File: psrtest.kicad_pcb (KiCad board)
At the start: 2 copper layers, 5 parts, among them J1 Conn_01x12, J2 Conn_01x12, J3 Conn_01x12, J4 Conn_01x12, U1 IS66WVE4M16EBLL-70BLI

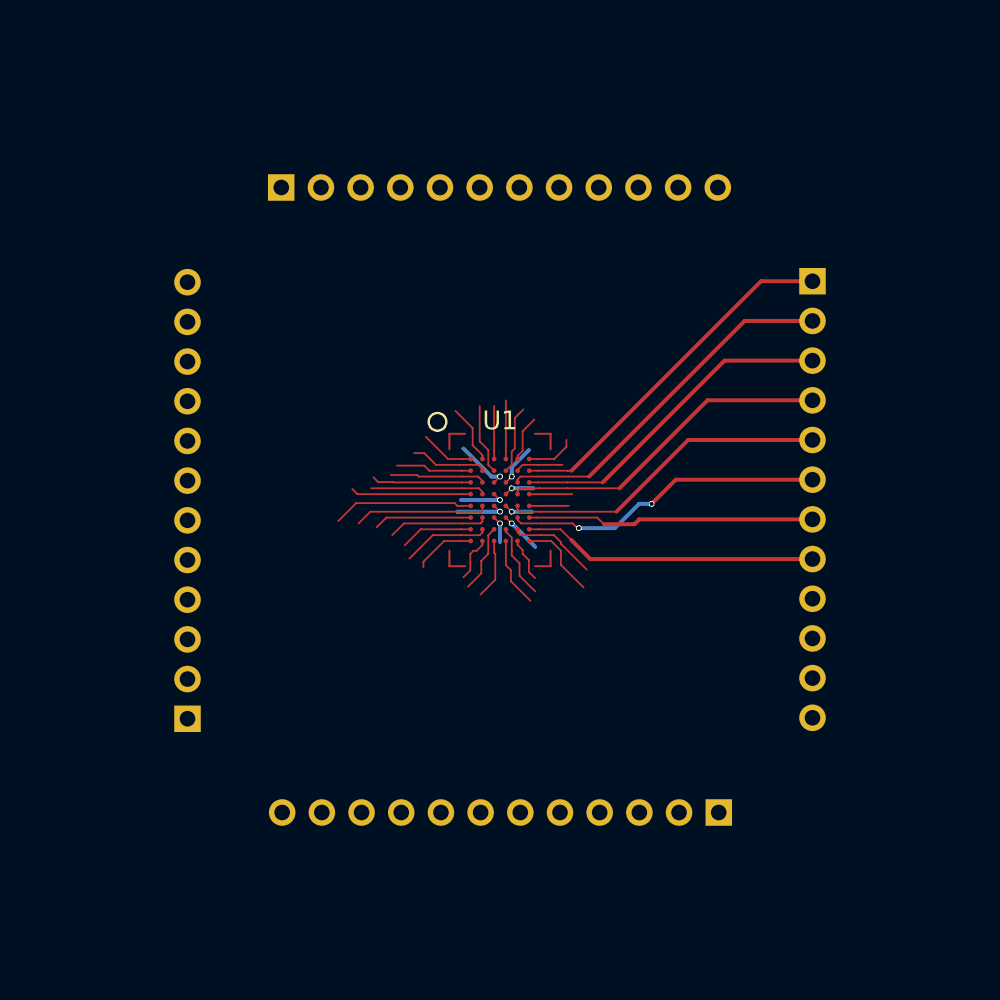
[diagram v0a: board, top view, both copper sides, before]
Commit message: Autoroute most signals.
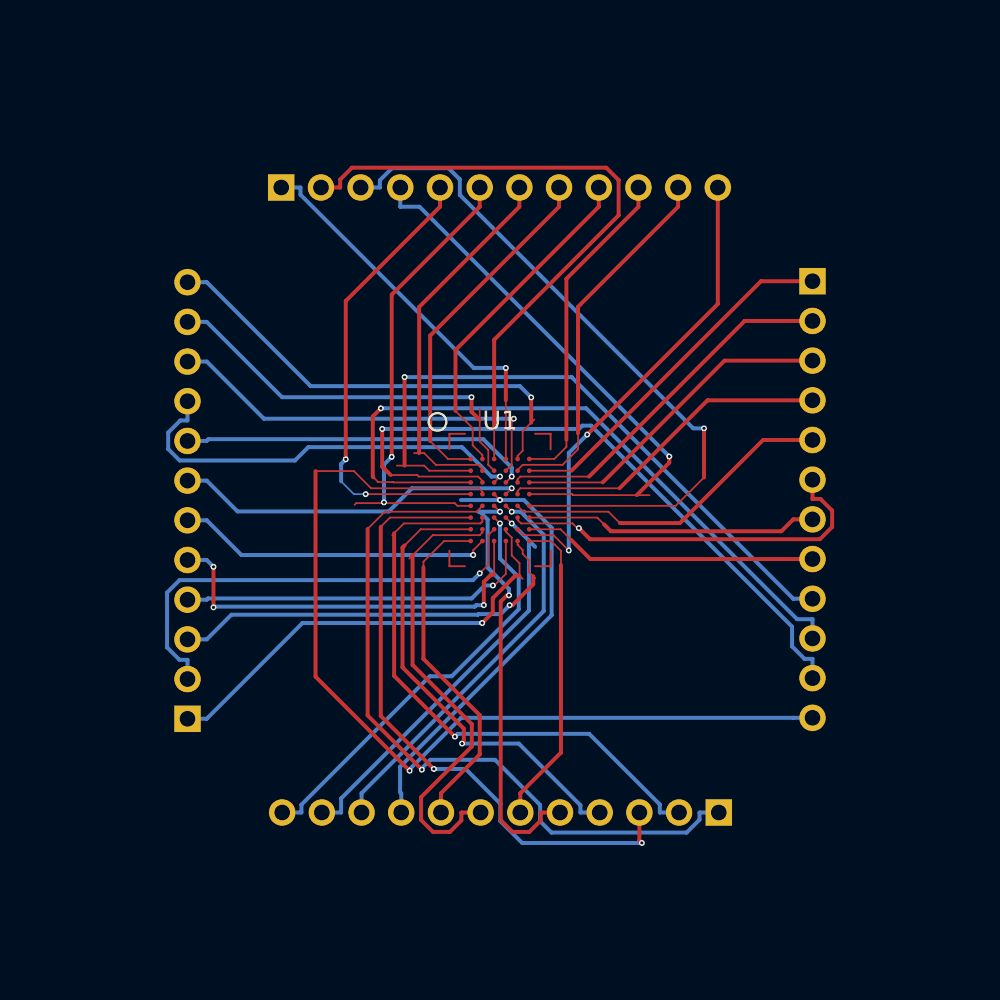
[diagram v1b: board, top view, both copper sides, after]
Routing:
- net /DQ11: track 7.37 -> 60.3 mm, vias 0 -> 1
- net /VSS: track 2.53 -> 45.3 mm, vias 0 -> 1
- net /DQ9: track 6.36 -> 45.5 mm, vias 0 -> 1
- net /DQ10: track 6.13 -> 45.1 mm, vias 0 -> 1
- net /DQ12: track 8.57 -> 47.5 mm, vias 0 -> 1
- net /A0: track 3.40 -> 41.4 mm
- net /DQ8: track 4.86 -> 42.5 mm, vias 0 -> 1
- net /DQ14: track 6.28 -> 40.9 mm, vias 0 -> 2
- net /VDD: track 2.75 -> 36.1 mm, vias 0 -> 1
- net /DQ13: track 6.39 -> 37.8 mm, vias 0 -> 1
- net /A2: track 2.97 -> 29.6 mm, vias 0 -> 1
- net /A17: track 3.03 -> 29.3 mm
- net /A12: track 4.37 -> 30.1 mm, vias 0 -> 1
- net /A14: track 1.73 -> 27.3 mm
- net /WE#: track 5.67 -> 31.0 mm, vias 0 -> 2
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
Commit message: Initial routing cleanup.
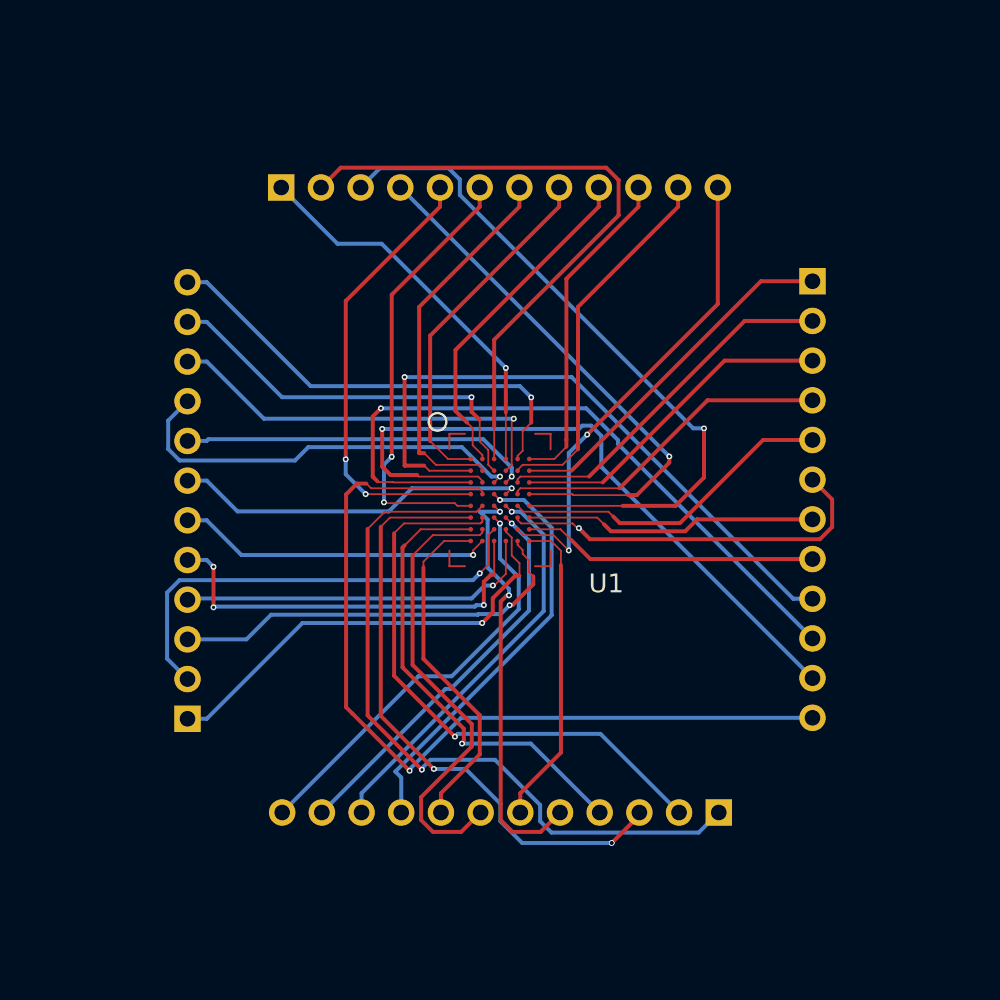
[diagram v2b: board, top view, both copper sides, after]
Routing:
- net /DQ11: track 60.3 -> 56.0 mm
- net /A17: track 29.3 -> 27.1 mm
- net /VDDQ: track 30.3 -> 28.4 mm
- net /VDD: track 36.1 -> 34.6 mm
- net /DQ14: track 40.9 -> 39.6 mm
- net /A15: track 26.3 -> 25.2 mm
- net /A3: track 26.2 -> 25.5 mm
- net /VSSQ: track 30.1 -> 29.4 mm
- net /A19: track 30.4 -> 29.8 mm

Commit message: Add some markings.
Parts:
- added REF**: Symbol_CC-PublicDomain_SilkScreenTop_Big, Symbols:Symbol_CC-PublicDomain_SilkScreenTop_Big, B.Cu at (109.8, 89.4)
- added REF***: ESD-Logo_8.9x8mm_SilkScreen, Symbols:ESD-Logo_8.9x8mm_SilkScreen, B.Cu at (109.8, 111.2)
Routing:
- net /VSSQ: vias 2 -> 3
- added copper zone on F.Cu, net /VSS
- added copper zone on B.Cu, net /VSSQ
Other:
- board outline added: 50 x 50 mm
- board text added: "0"
- board text added: "1"
- board text added: "10"
- board text added: "11"
- board text added: "12"
- board text added: "13"
- board text added: "14"
- board text added: "15"
- board text added: "16"
- board text added: "17"
- board text added: "18"
- board text added: "19"
- board text added: "2"
- board text added: "20"
- board text added: "3"
- board text added: "4"
- board text added: "5"
- board text added: "6"
- board text added: "7"
- board text added: "8"
- board text added: "9"
- board text added: "A0"
- board text added: "A21"
- board text added: "CE#"
- board text added: "DQ0"
- board text added: "DQ15"
- board text added: "LB#"
- board text added: "OE#"
- board text added: "PSRAM Test V1"
- board text added: "UB#"
- board text added: "VDD"
- board text added: "VDDQ"
- board text added: "VSS"
- board text added: "VSSQ"
- board text added: "WE#"
- board text added: "ZZ#"

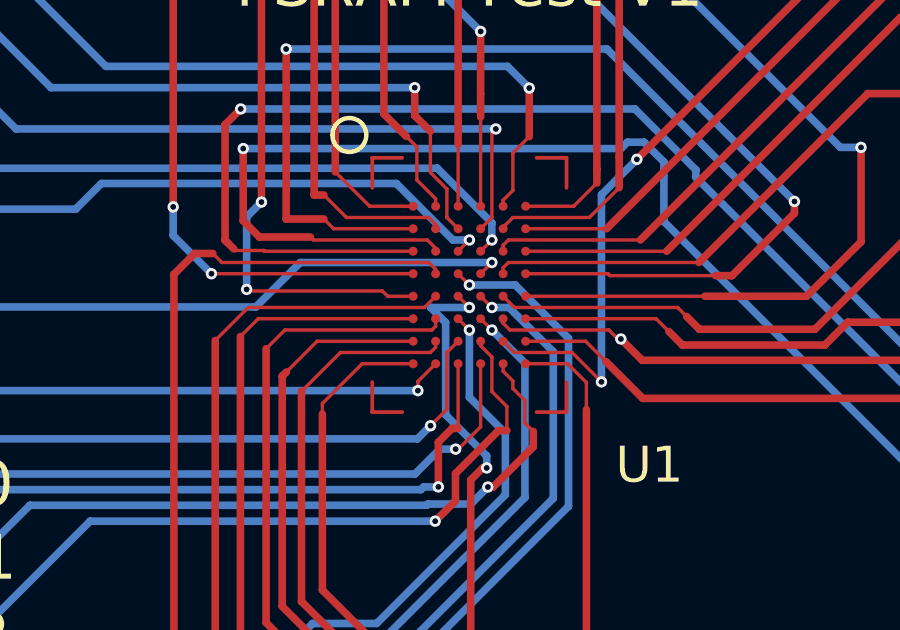
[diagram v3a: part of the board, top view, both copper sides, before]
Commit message: Fix a kink in a single trace.
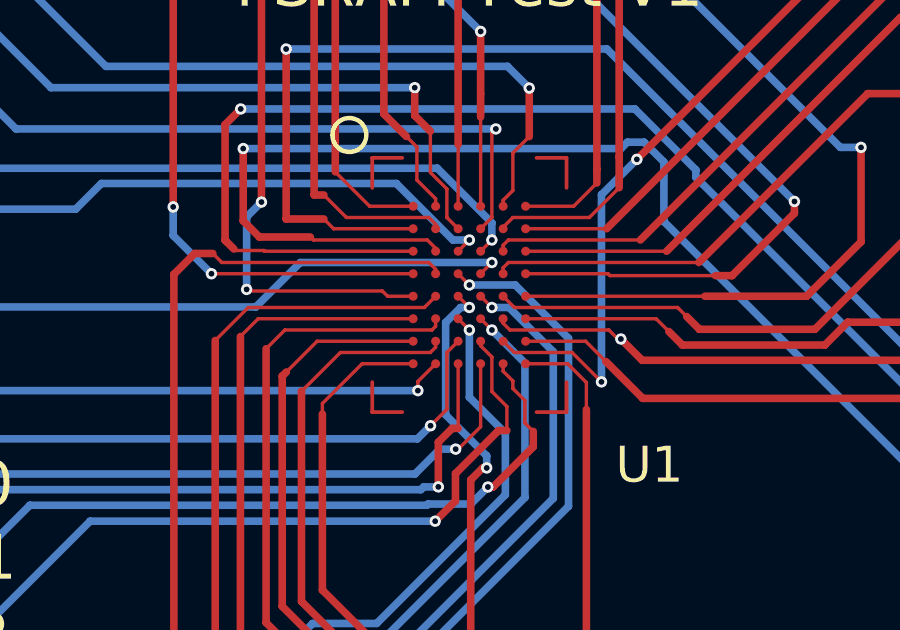
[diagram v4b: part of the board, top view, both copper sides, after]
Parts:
- moved REF*** 2.21 mm to (108.8, 109.2)
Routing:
- net /A21: track 27.3 -> 26.3 mm
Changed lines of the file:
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@@
   )
   (module Symbols:ESD-Logo_8.9x8mm_SilkScreen (layer B.Cu)
-    (at 109.8 111.15)
+    (at 108.75 109.2)
     (descr "Electrostatic discharge Logo")
     (tags "Logo ESD")
@@
   (via (at 100 100) (size 0.381) (layers F.Cu B.Cu) (net 20))
   (segment (start 99.625 99.625) (end 100 100) (width 0.1144) (layer F.Cu) (net 20) (status 10))
+  (segment (start 99.2088 101.2507) (end 99.7095 100.75) (width 0.254) (layer B.Cu) (net 21))
+  (segment (start 99.7095 100.75) (end 100 100.75) (width 0.254) (layer B.Cu) (net 21))
   (segment (start 100.5773 106.0983) (end 100.4437 106.0983) (width 0.254) (layer F.Cu) (net 21))
   (segment (start 100.4437 106.0983) (end 100.0451 106.4969) (width 0.254) (layer F.Cu) (net 21))
@@
   (via (at 100.5773 106.0983) (size 0.381) (layers F.Cu B.Cu) (net 21))
   (segment (start 99.625 100.375) (end 100 100.75) (width 0.1144) (layer F.Cu) (net 21) (status 10))
-  (segment (start 100 100.75) (end 98.7081 100.75) (width 0.254) (layer B.Cu) (net 21))
   (segment (start 100.5773 105.6962) (end 100.5773 106.0983) (width 0.254) (layer B.Cu) (net 21))
   (segment (start 99.2088 104.3277) (end 100.5773 105.6962) (width 0.254) (layer B.Cu) (net 21))
   (segment (start 99.2088 101.2507) (end 99.2088 104.3277) (width 0.254) (layer B.Cu) (net 21))
-  (segment (start 98.7081 100.75) (end 99.2088 101.2507) (width 0.254) (layer B.Cu) (net 21))
   (segment (start 100 101.5) (end 100 103.7428) (width 0.254) (layer B.Cu) (net 22))
   (segment (start 100 103.7428) (end 101.1997 104.9425) (width 0.254) (layer B.Cu) (net 22))

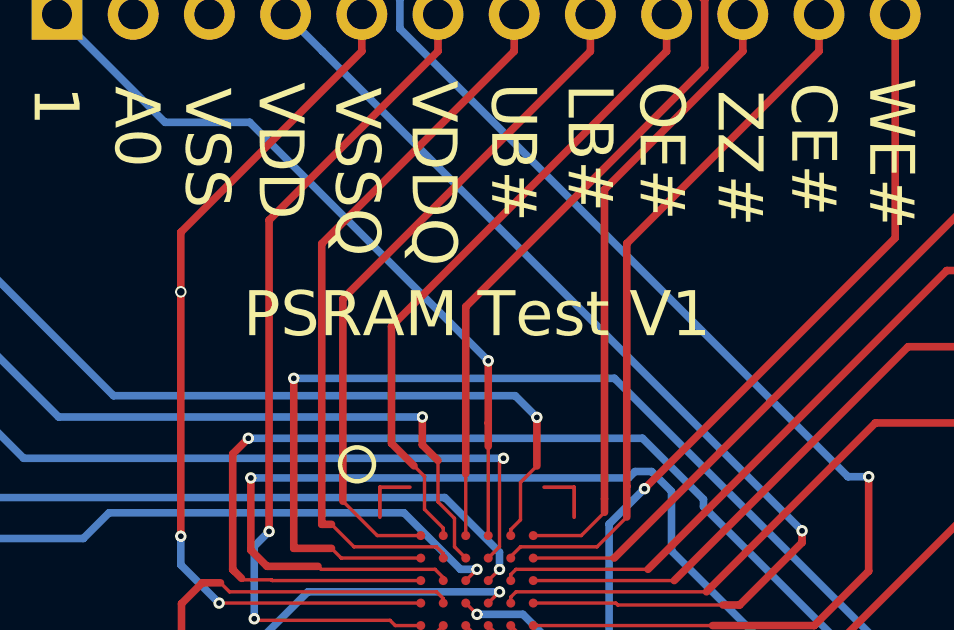
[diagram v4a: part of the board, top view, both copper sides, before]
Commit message: Actually this is V0. Also mark issue date.
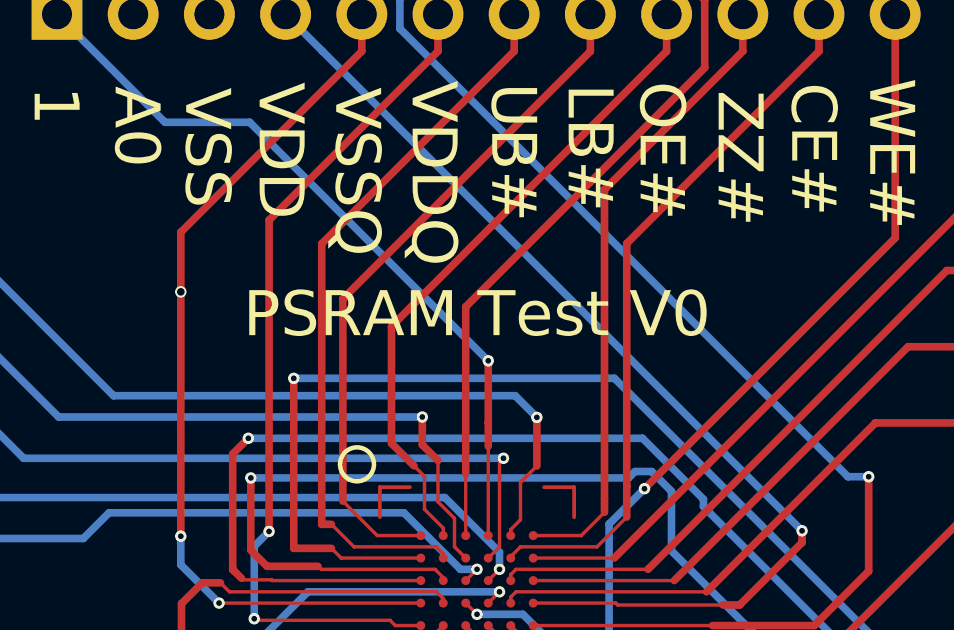
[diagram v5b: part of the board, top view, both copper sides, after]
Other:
- board text added: "PSRAM Test V0"
- board text removed: "PSRAM Test V1"
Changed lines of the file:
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@@
     (effects (font (size 1.5 1.5) (thickness 0.3)))
   )
-  (gr_text "PSRAM Test V1" (at 100 90) (layer F.SilkS)
+  (gr_text "PSRAM Test V0" (at 100 90) (layer F.SilkS)
     (effects (font (size 1.5 1.5) (thickness 0.3)))
   )
